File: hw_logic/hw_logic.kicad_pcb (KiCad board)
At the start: 2 copper layers, 62.2 x 38.1 mm, 10 parts, among them P1 CONN_01X10, SW13 SW_PUSH, U1 LEO_PRO_MICRO, U2 IS25LQ, U3 USB_HOST_SHIELD_MINI

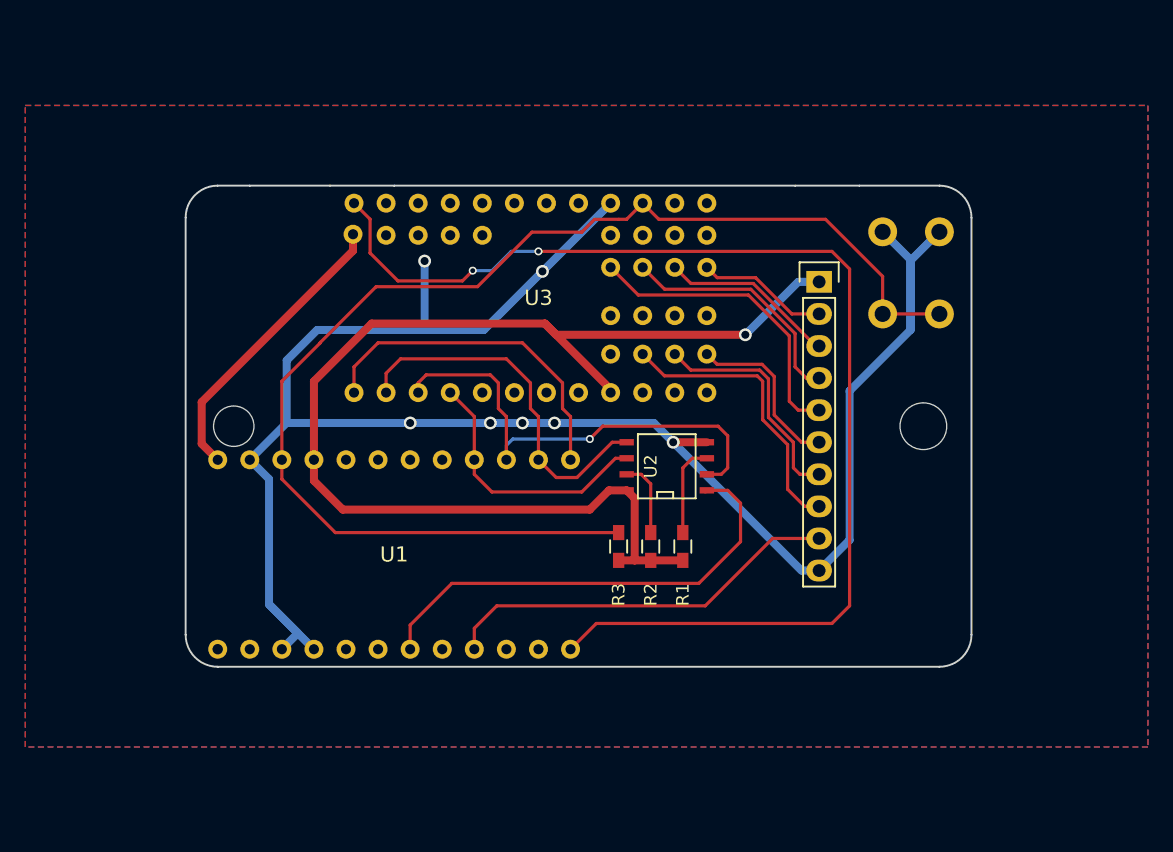
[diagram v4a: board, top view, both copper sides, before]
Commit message: revamp boards (for assembled height)
flip logic over so that it can mate closely with key; reset button moves
to same side as all the other parts; board assembly down to ~16mm high
and assembly more easily lends itself to angling for even less height at
the front for slightly more in the back
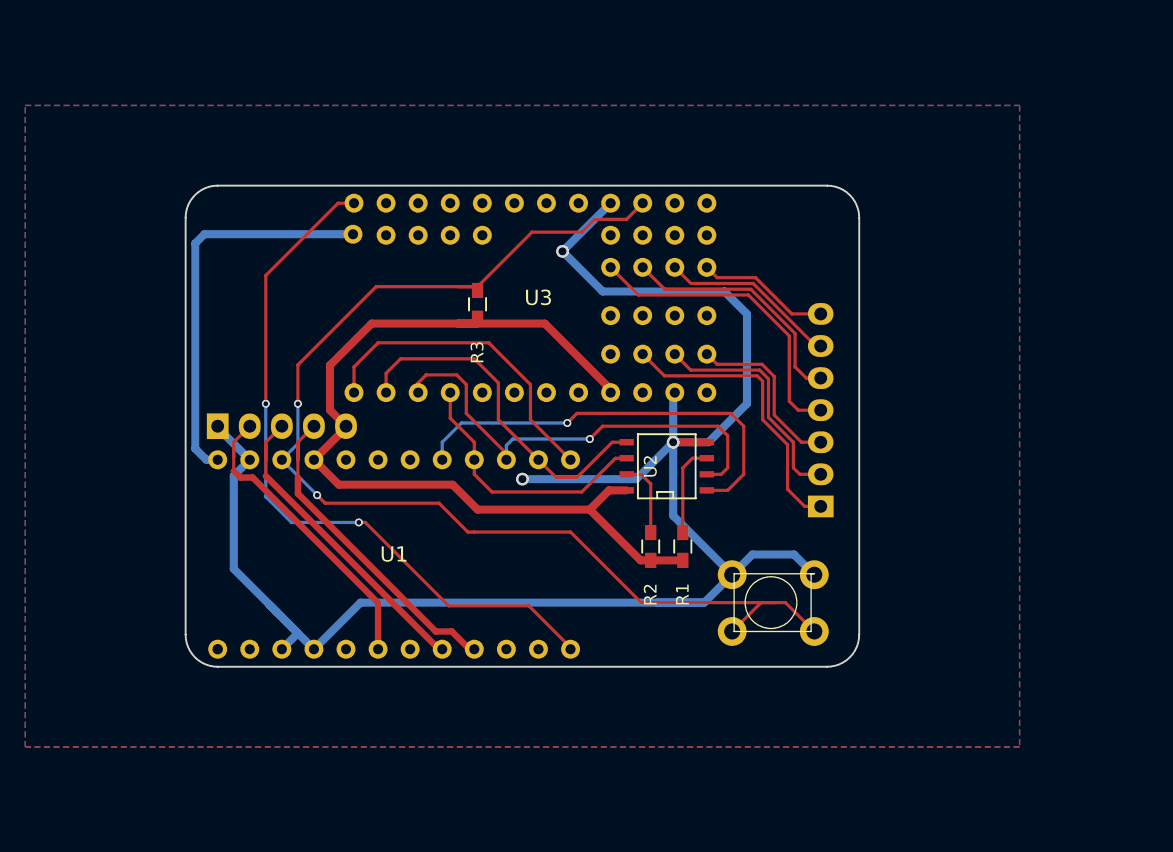
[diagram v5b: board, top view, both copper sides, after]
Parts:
- removed REF**: MountingHole_3.7mm, Mounting_Holes:MountingHole_3.7mm
- removed REF**: MountingHole_3.2mm_M3, Mounting_Holes:MountingHole_3.2mm_M3
- added P2: CONN_01X07, Pin_Headers:Pin_Header_Straight_1x07, B.Cu at (75.7, 50.8)
- P1: value CONN_01X10 -> CONN_01X05; footprint Pin_Headers:Pin_Header_Straight_1x10 -> Pin_Headers:Pin_Header_Straight_1x05; moved to B.Cu
- SW13: moved to F.Cu
- moved P1 49.0 mm to (27.9, 44.5), turned to 270 degrees
- moved SW13 27.0 mm to (75.2, 60.7), turned to 180 degrees
- moved R3 22.2 mm to (48.5, 34.8)
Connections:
- P1 pad 1: +3V3 -> GND
- P1 pad 2: /GO0 -> /LED_B
- P1 pad 3: /GO1 -> /LED_G
- P1 pad 4: /GO2 -> /LED_R
- P1 pad 5: /GO3 -> +3V3
- U1 pad 17: (no net) -> /FLASH_SS
- U1 pad 6: (no net) -> /LED_B
- U1 pad 7: /FLASH_SS -> (no net)
- U1 pad 8: (no net) -> /LED_G
- U1 pad 9: /LED_MACRO -> /LED_R
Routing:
- net /USB_INT: track 95.1 -> 56.1 mm
- net /LED_MACRO: track 31.9 -> 0.00 mm
- net /LED_R: track 0.00 -> 26.6 mm
- net /LED_G: track 0.00 -> 25.3 mm
- net /LED_B: track 0.00 -> 24.4 mm
- net +3V3: track 97.1 -> 73.7 mm, vias 1 -> 0
- net GND: track 156.7 -> 143.6 mm, vias 7 -> 3
- net +5V: track 23.4 -> 31.2 mm
- net /RST: track 99.5 -> 94.5 mm, vias 0 -> 2
- net /FLASH_SS: track 37.1 -> 34.1 mm, vias 0 -> 1
- net /MISO: track 38.0 -> 35.9 mm
- net /USB_SS: track 27.0 -> 25.4 mm
- net /MOSI: track 29.3 -> 27.8 mm
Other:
- board size 62.2 x 38.1 mm -> 53.3 x 38.1 mm

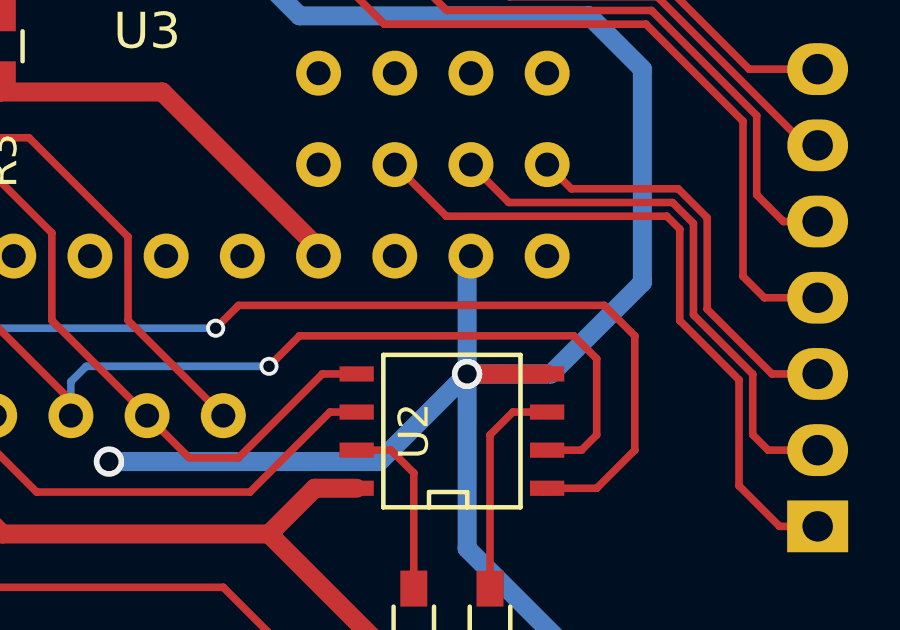
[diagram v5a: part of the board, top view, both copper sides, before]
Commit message: final PCB revisions
plus the start of a case to hold them
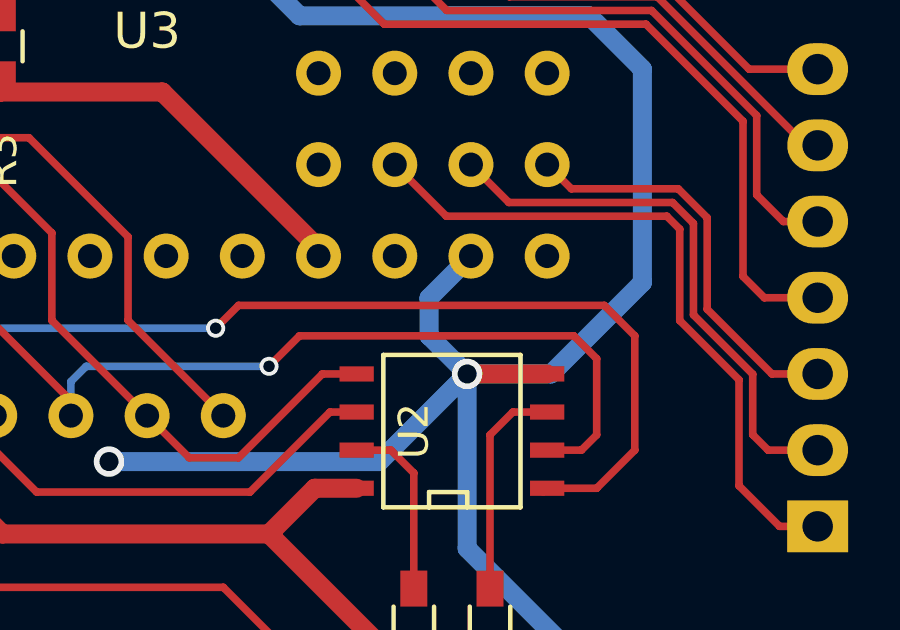
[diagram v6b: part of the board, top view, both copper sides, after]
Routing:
- net GND: track 143.6 -> 144.8 mm
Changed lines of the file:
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@@
     (links 40)
     (no_connects 0)
-    (area 25.324999 25.324999 78.815001 63.575001)
+    (area 12.7 19.05 91.440001 69.850001)
     (thickness 1.6)
     (drawings 9)
-    (tracks 232)
+    (tracks 234)
     (zones 0)
     (modules 9)
@@
   )
   (setup
-    (last_trace_width 0.508)
+    (last_trace_width 0.254)
     (user_trace_width 0.508)
     (trace_clearance 0.2032)
@@
   (segment (start 40.132 36.322) (end 36.83 39.624) (width 0.635) (layer F.Cu) (net 1))
   (segment (start 36.83 41.148) (end 36.83 39.624) (width 0.635) (layer F.Cu) (net 1))
+  (segment (start 64.008 45.72) (end 62.738 44.45) (width 0.635) (layer B.Cu) (net 2))
+  (segment (start 62.738 43.187) (end 64.135 41.79) (width 0.635) (layer B.Cu) (net 2) (status 800000))
+  (segment (start 62.738 44.45) (end 62.738 43.187) (width 0.635) (layer B.Cu) (net 2))
   (segment (start 75.184 56.2102) (end 73.5838 54.61) (width 0.635) (layer B.Cu) (net 2))
   (segment (start 70.2818 54.61) (end 68.6816 56.2102) (width 0.635) (layer B.Cu) (net 2))
@@
   (segment (start 58.42 33.782) (end 68.072 33.782) (width 0.635) (layer B.Cu) (net 2))
   (segment (start 64.135 41.79) (end 64.008 41.917) (width 0.635) (layer B.Cu) (net 2) (status 30))
-  (segment (start 64.008 41.917) (end 64.008 45.72) (width 0.635) (layer B.Cu) (net 2) (status 10))
   (segment (start 68.6816 56.2102) (end 66.4718 58.42) (width 0.635) (layer B.Cu) (net 2) (status 10))
   (segment (start 66.4718 58.42) (end 62.738 58.42) (width 0.635) (layer B.Cu) (net 2))

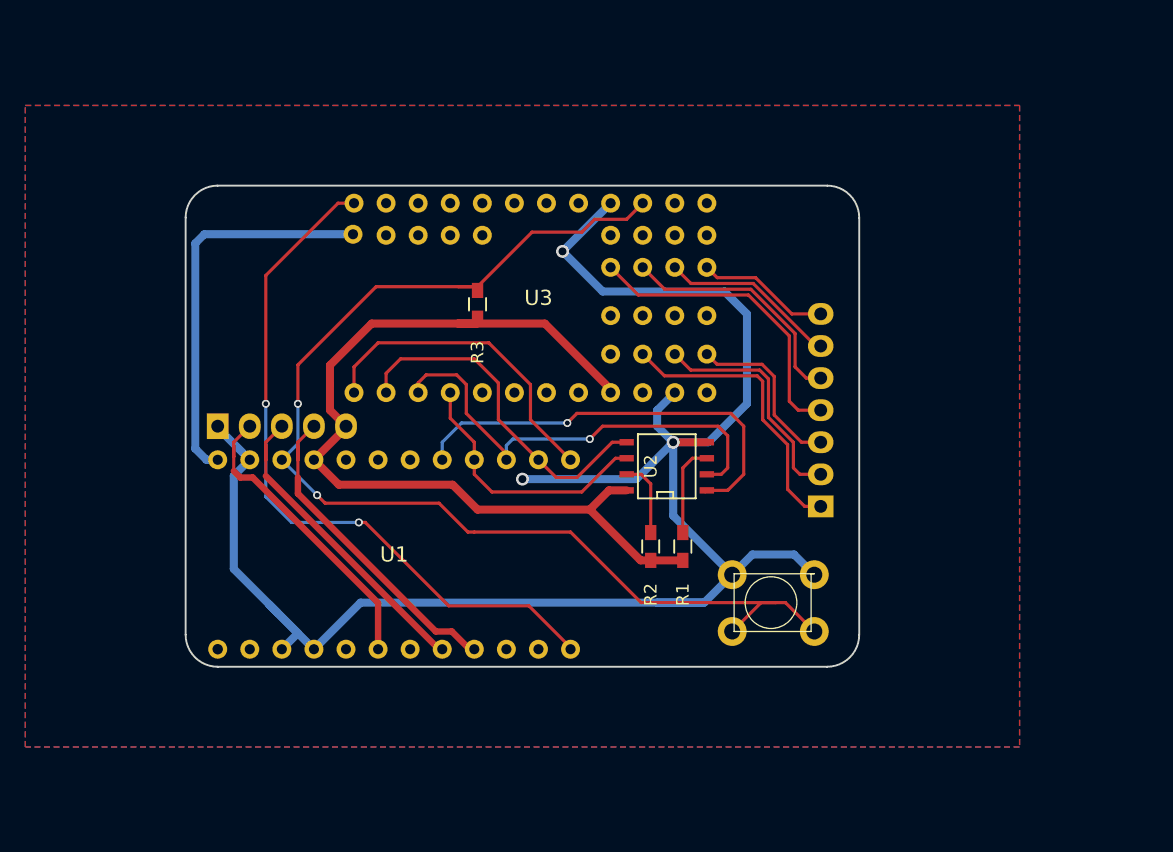
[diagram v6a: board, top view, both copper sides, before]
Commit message: Logic PCB: Fix connector P2 position, swap LED power line.
A better fix would also swap around the LED on the "key" board, but this reduces bodge needs without respinning that board.
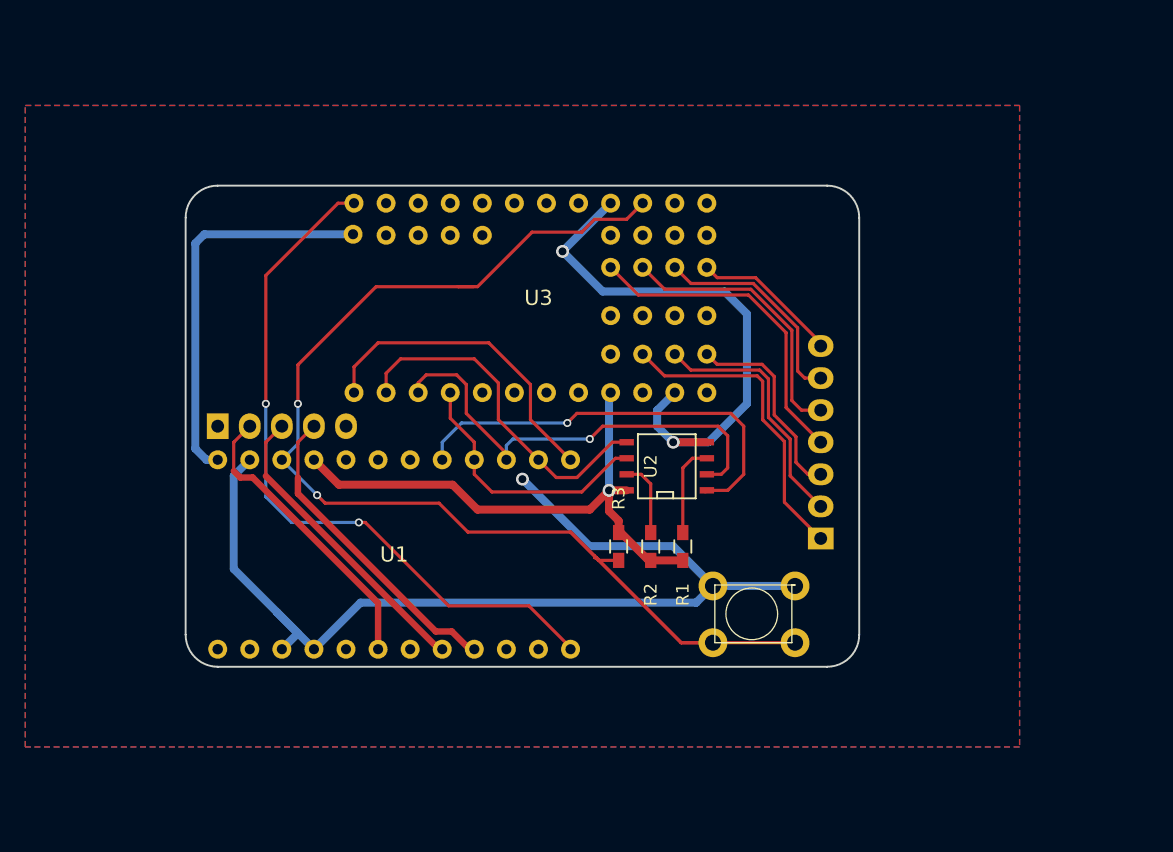
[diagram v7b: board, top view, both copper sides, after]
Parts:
- moved R3 22.2 mm to (59.7, 54.0), turned to 270 degrees
- moved P2 2.54 mm to (75.7, 53.3)
- moved SW13 1.76 mm to (73.7, 61.6)
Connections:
- P1 pad 1: GND -> (no net)
- P1 pad 5: +3V3 -> GND
- U3 pad 11: GND -> (no net)
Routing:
- net +3V3: track 73.7 -> 45.1 mm, vias 0 -> 1
- net GND: track 144.8 -> 125.5 mm
- net /RST: track 94.5 -> 105.5 mm
- net /GO1: track 14.0 -> 17.2 mm
- net /GO2: track 19.2 -> 22.0 mm
- net /GI0: track 13.6 -> 15.9 mm
- net /GI2: track 22.8 -> 24.7 mm
- net /GI1: track 18.3 -> 20.0 mm
- net /GO3: track 24.2 -> 25.9 mm
- net /GO0: track 11.0 -> 12.4 mm
- net /LED_R: track 26.6 -> 25.5 mm
- net /LED_G: track 25.3 -> 24.1 mm
- net /LED_B: track 24.4 -> 23.5 mm

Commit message: Sub-boards on silkscreen layer.
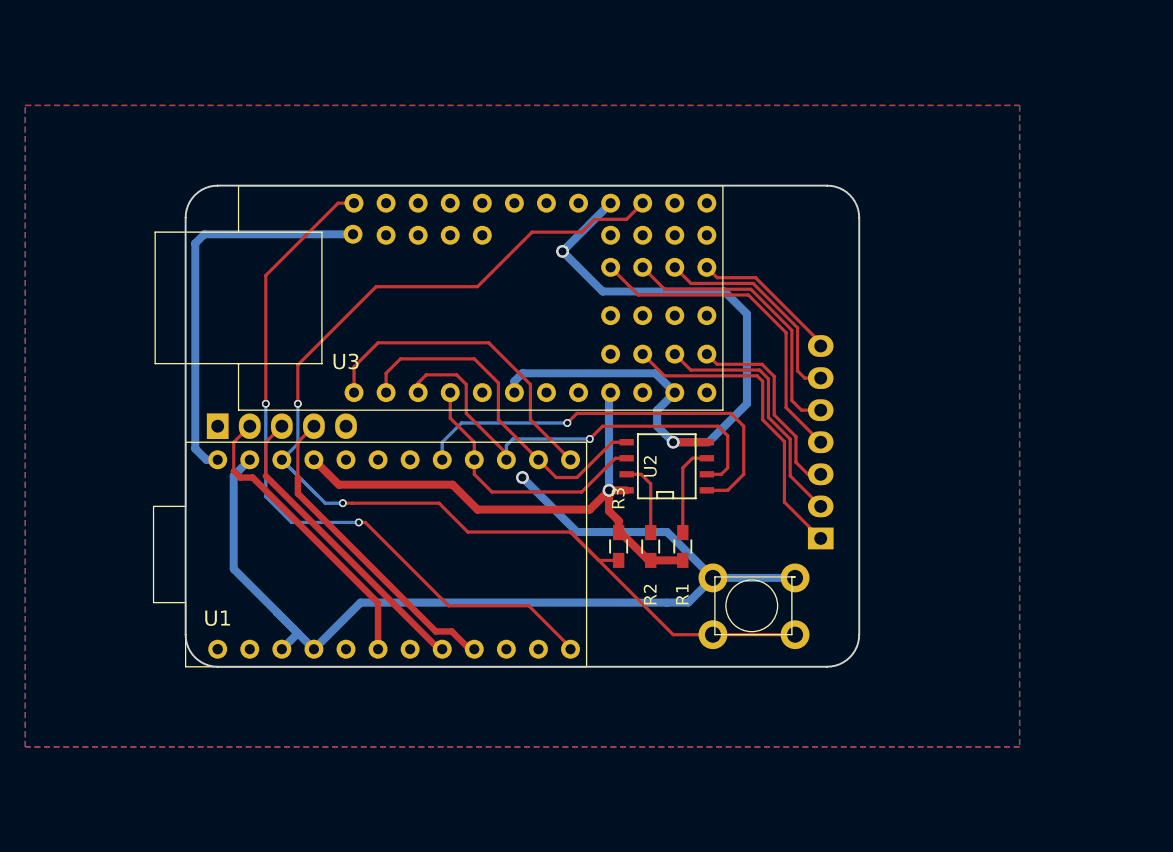
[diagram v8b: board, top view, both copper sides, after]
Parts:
- moved SW13 0.63 mm to (73.7, 61.0)
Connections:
- U3 pad 11: (no net) -> GND
- U3 pad 6: (no net) -> GND
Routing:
- net GND: track 125.5 -> 140.0 mm
- net /RST: track 105.5 -> 95.7 mm
